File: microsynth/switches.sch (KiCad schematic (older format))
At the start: 35 parts, among them SW12 SOURCE, SW13 THUMBWEEL, SW14 SW_SPDT, SW15 SW_SPDT, SW16 SW_SPDT, SW17 SW_SPDT, SW2 RANGE, SW21 SW_Rotary2x6, SW3 SW_DPTT_SELECTOR, SW4 SW_DPTT_SELECTOR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

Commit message: Tidy up, name switches, proper footprints for all trimmers
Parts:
- RV4, RV7: footprint Potentiometers:Potentiometer_WirePads_Small -> Potentiometers:Potentiometer_Trimmer_Bourns_PV36W
- SW12, SW13, SW3, SW4, SW6: footprint Buttons_Switches_ThroughHole:L203011MS02Q -> Buttons_Switches_ThroughHole:G-1128S-1110
- SW14, SW15, SW16, SW17, SW5: footprint 4ms:SPDT_KIT -> Buttons_Switches_ThroughHole:GF-624-6014
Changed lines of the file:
@@
 F 0 "SW6" H 6294 3079 50  0000 L CNN
 F 1 "SW_DPTT_SELECTOR" H 6294 2988 50  0000 L CNN
-F 2 "Buttons_Switches_ThroughHole:L203011MS02Q" H 6100 2950 50  0001 C CNN
+F 2 "Buttons_Switches_ThroughHole:G-1128S-1110" H 6100 2950 50  0001 C CNN
 F 3 "" H 6100 2950 50  0001 C CNN
 	2    6100 2950
@@
 F 0 "SW3" H 7594 1338 50  0000 L CNN
 F 1 "SW_DPTT_SELECTOR" H 7594 1247 50  0000 L CNN
-F 2 "Buttons_Switches_ThroughHole:L203011MS02Q" H 7400 1350 50  0001 C CNN
+F 2 "Buttons_Switches_ThroughHole:G-1128S-1110" H 7400 1350 50  0001 C CNN
 F 3 "" H 7400 1350 50  0001 C CNN
 	1    7400 1350
@@
 F 0 "SW3" H 7594 1379 50  0000 L CNN
 F 1 "SW_DPTT_SELECTOR" H 7594 1288 50  0000 L CNN
-F 2 "Buttons_Switches_ThroughHole:L203011MS02Q" H 7400 1250 50  0001 C CNN
+F 2 "Buttons_Switches_ThroughHole:G-1128S-1110" H 7400 1250 50  0001 C CNN
 F 3 "" H 7400 1250 50  0001 C CNN
 	2    7400 1250
@@
 F 0 "SW4" H 9344 1338 50  0000 L CNN
 F 1 "SW_DPTT_SELECTOR" H 9344 1247 50  0000 L CNN
-F 2 "Buttons_Switches_ThroughHole:L203011MS02Q" H 9150 1350 50  0001 C CNN
+F 2 "Buttons_Switches_ThroughHole:G-1128S-1110" H 9150 1350 50  0001 C CNN
 F 3 "" H 9150 1350 50  0001 C CNN
 	1    9150 1350
@@
 F 0 "SW4" H 9344 1379 50  0000 L CNN
 F 1 "SW_DPTT_SELECTOR" H 9344 1288 50  0000 L CNN
-F 2 "Buttons_Switches_ThroughHole:L203011MS02Q" H 9150 1250 50  0001 C CNN
+F 2 "Buttons_Switches_ThroughHole:G-1128S-1110" H 9150 1250 50  0001 C CNN
 F 3 "" H 9150 1250 50  0001 C CNN
 	2    9150 1250
@@
 F 0 "SW5" V 10604 1112 50  0000 R CNN
 F 1 "SW_SPDT" V 10695 1112 50  0000 R CNN
-F 2 "4ms:SPDT_KIT" H 10650 1300 50  0001 C CNN
+F 2 "Buttons_Switches_ThroughHole:GF-624-6014" H 10650 1300 50  0001 C CNN
 F 3 "~" H 10650 1300 50  0001 C CNN
 	1    10650 1300
@@
 F 0 "RV4" V 3735 5750 50  0000 C CNN
 F 1 "10k" V 3644 5750 50  0000 C CNN
-F 2 "Potentiometers:Potentiometer_WirePads_Small" H 3850 5750 50  0001 C CNN
+F 2 "Potentiometers:Potentiometer_Trimmer_Bourns_PV36W" H 3850 5750 50  0001 C CNN
 F 3 "~" H 3850 5750 50  0001 C CNN
 	1    3850 5750
@@
 F 0 "RV7" V 4735 6150 50  0000 C CNN
 F 1 "47k" V 4644 6150 50  0000 C CNN
-F 2 "Potentiometers:Potentiometer_WirePads_Small" H 4850 6150 50  0001 C CNN
+F 2 "Potentiometers:Potentiometer_Trimmer_Bourns_PV36W" H 4850 6150 50  0001 C CNN
 F 3 "~" H 4850 6150 50  0001 C CNN
 	1    4850 6150
@@
 F 0 "SW6" H 2894 2738 50  0000 L CNN
 F 1 "SW_DPTT_SELECTOR" H 2894 2647 50  0000 L CNN
-F 2 "Buttons_Switches_ThroughHole:L203011MS02Q" H 2700 2750 50  0001 C CNN
+F 2 "Buttons_Switches_ThroughHole:G-1128S-1110" H 2700 2750 50  0001 C CNN
 F 3 "" H 2700 2750 50  0001 C CNN
 	1    2700 2750
@@
 F 0 "SW17" H 3600 2635 50  0000 C CNN
 F 1 "SW_SPDT" H 3600 2544 50  0000 C CNN
-F 2 "4ms:SPDT_KIT" H 3600 2350 50  0001 C CNN
+F 2 "Buttons_Switches_ThroughHole:GF-624-6014" H 3600 2350 50  0001 C CNN
 F 3 "~" H 3600 2350 50  0001 C CNN
 	1    3600 2350
@@
 F 0 "SW16" H 3600 2135 50  0000 C CNN
 F 1 "SW_SPDT" H 3600 2044 50  0000 C CNN
-F 2 "4ms:SPDT_KIT" H 3600 1850 50  0001 C CNN
+F 2 "Buttons_Switches_ThroughHole:GF-624-6014" H 3600 1850 50  0001 C CNN
 F 3 "~" H 3600 1850 50  0001 C CNN
 	1    3600 1850
@@
 F 0 "SW15" H 3600 1635 50  0000 C CNN
 F 1 "SW_SPDT" H 3600 1544 50  0000 C CNN
-F 2 "4ms:SPDT_KIT" H 3600 1350 50  0001 C CNN
+F 2 "Buttons_Switches_ThroughHole:GF-624-6014" H 3600 1350 50  0001 C CNN
 F 3 "~" H 3600 1350 50  0001 C CNN
 	1    3600 1350
@@
 F 0 "SW14" H 3600 1135 50  0000 C CNN
 F 1 "SW_SPDT" H 3600 1044 50  0000 C CNN
-F 2 "4ms:SPDT_KIT" H 3600 850 50  0001 C CNN
+F 2 "Buttons_Switches_ThroughHole:GF-624-6014" H 3600 850 50  0001 C CNN
 F 3 "~" H 3600 850 50  0001 C CNN
 	1    3600 850
@@
 F 0 "SW12" H 5594 4488 50  0000 L CNN
 F 1 "SOURCE" H 5594 4397 50  0000 L CNN
-F 2 "Buttons_Switches_ThroughHole:L203011MS02Q" H 5400 4500 50  0001 C CNN
+F 2 "Buttons_Switches_ThroughHole:G-1128S-1110" H 5400 4500 50  0001 C CNN
 F 3 "" H 5400 4500 50  0001 C CNN
 	1    5400 4500
@@
 F 0 "SW12" H 5594 4629 50  0000 L CNN
 F 1 "SOURCE" H 5594 4538 50  0000 L CNN
-F 2 "Buttons_Switches_ThroughHole:L203011MS02Q" H 5400 4500 50  0001 C CNN
+F 2 "Buttons_Switches_ThroughHole:G-1128S-1110" H 5400 4500 50  0001 C CNN
 F 3 "" H 5400 4500 50  0001 C CNN
 	2    5400 4500
@@
 F 0 "SW13" H 7394 4438 50  0000 L CNN
 F 1 "THUMBWEEL" H 7394 4347 50  0000 L CNN
-F 2 "Buttons_Switches_ThroughHole:L203011MS02Q" H 7200 4450 50  0001 C CNN
+F 2 "Buttons_Switches_ThroughHole:G-1128S-1110" H 7200 4450 50  0001 C CNN
 F 3 "" H 7200 4450 50  0001 C CNN
 	1    7200 4450
@@
 F 0 "SW13" H 7394 4579 50  0000 L CNN
 F 1 "THUMBWEEL" H 7394 4488 50  0000 L CNN
-F 2 "Buttons_Switches_ThroughHole:L203011MS02Q" H 7200 4450 50  0001 C CNN
+F 2 "Buttons_Switches_ThroughHole:G-1128S-1110" H 7200 4450 50  0001 C CNN
 F 3 "" H 7200 4450 50  0001 C CNN
 	2    7200 4450

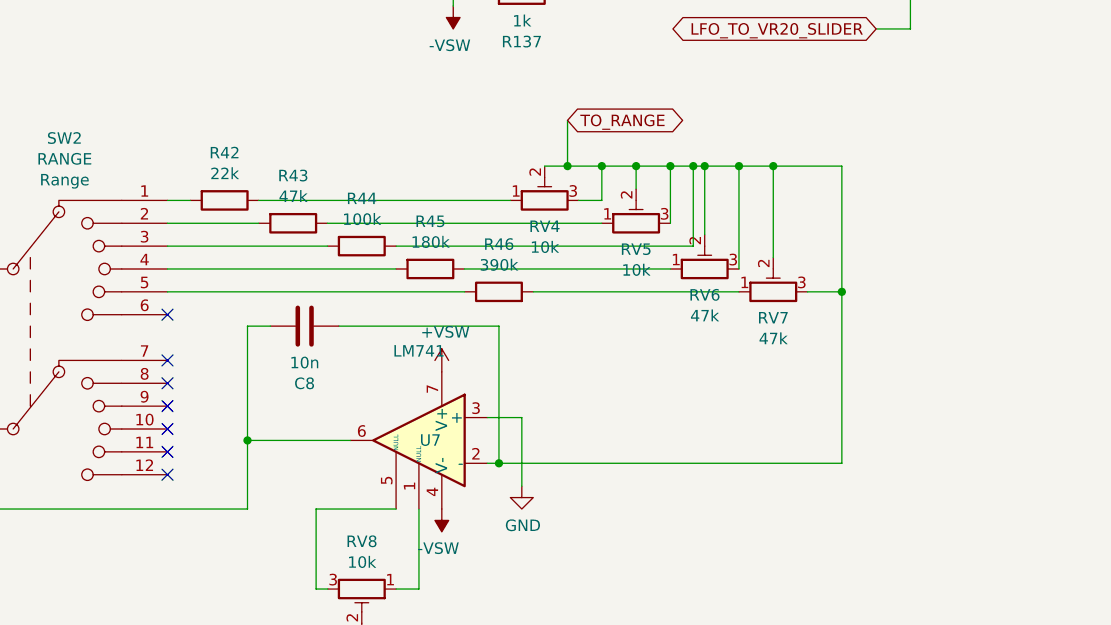
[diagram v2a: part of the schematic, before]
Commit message: Replace switches in schematic, add extra octave to VCO
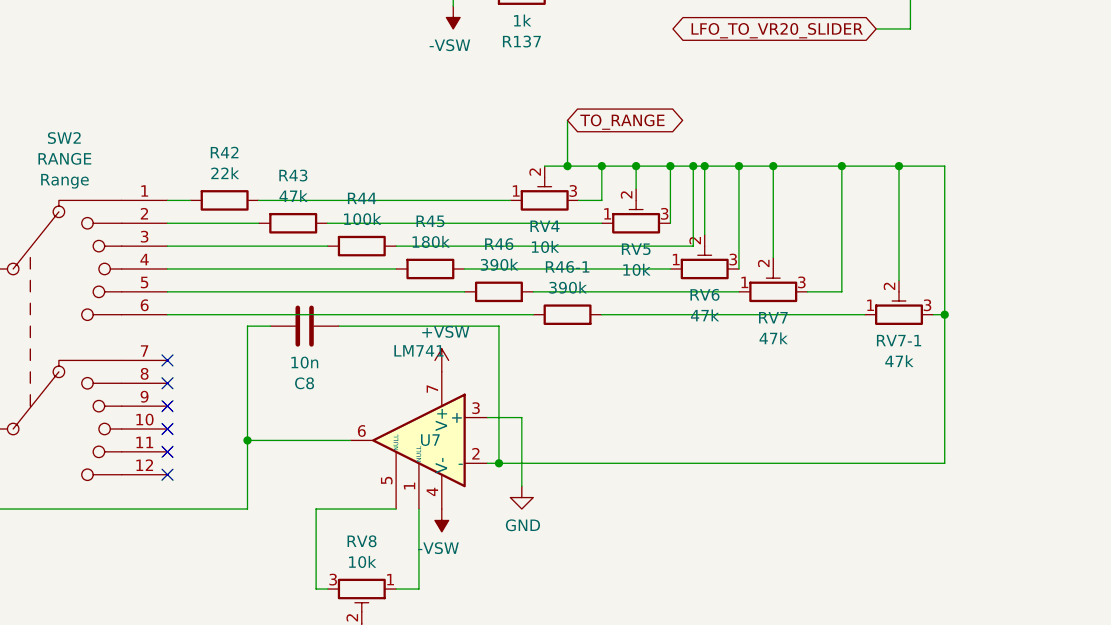
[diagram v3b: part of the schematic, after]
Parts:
- added R46-1: 390k, Resistor_THT:R_Axial_DIN0207_L6.3mm_D2.5mm_P10.16mm_Horizontal, symbol Device:R
- added RV7-1: 47k, Potentiometers:Potentiometer_Trimmer_Bourns_PV36W, symbol Device:R_POT_TRIM
- SW21: footprint MyKi_TH_Panel_Controls:SW_Rotary4+12 -> MyKi_TH_Panel_Controls:LORINCK1049
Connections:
- net TO_RANGE: now also RV7-1.2, RV7-1.3
- net at SW2.6: now also R46-1.1
- new net: R46-1.2, RV7-1.1
- no-connect marks 28 -> 27
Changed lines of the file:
@@
 Wire Wire Line
 	1200 6050 1300 6050
-NoConn ~ 2200 6250
 $Comp
 L Device:R R42
@@
 	2550 7100 2550 6800
 Connection ~ 2550 6800
-Wire Wire Line
-	5150 6150 5150 5600
-Wire Wire Line
-	5150 6900 3650 6900
-Connection ~ 5150 6150
 Connection ~ 3650 6900
 Wire Wire Line
@@
 F 0 "SW21" H 1850 2631 50  0000 C CNN
 F 1 "SW_Rotary2x6" H 1850 2540 50  0000 C CNN
-F 2 "MyKi_TH_Panel_Controls:SW_Rotary4+12" H 1700 2450 50  0001 C CNN
+F 2 "MyKi_TH_Panel_Controls:LORINCK1049" H 1700 2450 50  0001 C CNN
 F 3 "http://cdn-reichelt.de/documents/datenblatt/C200/DS-Serie%23LOR.pdf" H 1700 2450 50  0001 C CNN
 	1    1800 1850
@@
 Connection ~ 5350 4700
 Connection ~ 5350 4300
-Wire Wire Line
-	5150 6150 5150 6900
-Wire Wire Line
-	5150 5600 4850 5600
 Connection ~ 4850 5600
 Wire Wire Line
@@
 Wire Wire Line
 	4750 4600 4750 4800
+$Comp
+L Device:R R46-1
+U 1 1 5EAE5FD2
+P 3950 6250
+F 0 "R46-1" V 4157 6250 50  0000 C CNN
+F 1 "390k" V 4066 6250 50  0000 C CNN
+F 2 "Resistor_THT:R_Axial_DIN0207_L6.3mm_D2.5mm_P10.16mm_Horizontal" V 3880 6250 50  0001 C CNN
+F 3 "~" H 3950 6250 50  0001 C CNN
+	1    3950 6250
+	0    -1   -1   0
+$EndComp
+Wire Wire Line
+	5600 5600 5600 6250
+Wire Wire Line
+	4850 5600 5150 5600
+Wire Wire Line
+	3650 6900 5600 6900
+Wire Wire Line
+	5150 6150 5150 5600
+Connection ~ 5150 5600
+Wire Wire Line
+	5150 5600 5400 5600
+$Comp
+L Device:R_POT_TRIM RV7-1
+U 1 1 5EB1EF45
+P 5400 6250
+F 0 "RV7-1" V 5285 6250 50  0000 C CNN
+F 1 "47k" V 5194 6250 50  0000 C CNN
+F 2 "Potentiometers:Potentiometer_Trimmer_Bourns_PV36W" H 5400 6250 50  0001 C CNN
+F 3 "~" H 5400 6250 50  0001 C CNN
+	1    5400 6250
+	0    -1   -1   0
+$EndComp
+Wire Wire Line
+	5400 6100 5400 5600
+Connection ~ 5400 5600
+Wire Wire Line
+	5400 5600 5600 5600
+Wire Wire Line
+	5550 6250 5600 6250
+Connection ~ 5600 6250
+Wire Wire Line
+	5600 6250 5600 6900
+Wire Wire Line
+	5250 6250 4100 6250
+Wire Wire Line
+	3800 6250 2200 6250
 $EndSCHEMATC

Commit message: Update datasheet for SW2
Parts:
- SW2: Product# (none) -> SR26NS1-2-6-M10-38R6
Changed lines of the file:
@@
 F 1 "RANGE" H 1750 7130 50  0000 C CNN
 F 2 "MyKi_TH_Panel_Controls:SW_Rotary4+12" H 1600 6950 50  0001 C CNN
-F 3 "http://cdn-reichelt.de/documents/datenblatt/C200/DS-Serie%23LOR.pdf" H 1600 6950 50  0001 C CNN
+F 3 "https://www.tme.eu/Document/ecc8d6706892f543e4658b0fb9f5b772/sr261112.pdf" H 1600 6950 50  0001 C CNN
 F 4 "Range" H 1750 7039 50  0000 C CNN "Label"
+F 5 "SR26NS1-2-6-M10-38R6" H 1700 6350 50  0001 C CNN "Product#"
 	1    1700 6350
 	1    0    0    -1

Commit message: Replace SW21 with 3p4t tayda
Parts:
- SW21: footprint MyKi_TH_Panel_Controls:LORINCK1049 -> Button_Switch_THT:SR2612F-0304-18R0B-D8-N; symbol Switch:SW_Rotary2x6 -> Switch:SW_Rotary3x4
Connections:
- net TO_VCA_C27: now also SW21.6; no longer SW21.8
- net TO_VCF_R120: now also SW21.5, SW21.8; no longer SW21.10, SW21.9
- no-connect marks 27 -> 28
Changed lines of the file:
@@
 	2400 2950 2550 2950
 Wire Wire Line
-	2400 2250 2400 2950
-Wire Wire Line
-	2200 2250 2400 2250
+	2400 2050 2400 2950
+Wire Wire Line
+	2200 2050 2400 2050
 $Comp
 L microsynth-rescue:SW_DPTT_SELECTOR-Switch SW6
@@
 	1    0    0    -1
 $EndComp
-NoConn ~ 1300 2450
-NoConn ~ 1300 2350
-NoConn ~ 1300 1750
-NoConn ~ 1300 1650
 NoConn ~ 3800 2450
 NoConn ~ 3800 1950
@@
 $EndComp
 Wire Wire Line
-	1150 1950 1300 1950
-Wire Wire Line
-	1300 2250 1150 2250
-$Comp
-L Switch:SW_Rotary2x6 SW21
-U 1 1 5E476048
-P 1800 1850
-F 0 "SW21" H 1850 2631 50  0000 C CNN
-F 1 "SW_Rotary2x6" H 1850 2540 50  0000 C CNN
-F 2 "MyKi_TH_Panel_Controls:LORINCK1049" H 1700 2450 50  0001 C CNN
-F 3 "http://cdn-reichelt.de/documents/datenblatt/C200/DS-Serie%23LOR.pdf" H 1700 2450 50  0001 C CNN
-	1    1800 1850
-	-1   0    0    -1
-$EndComp
+	1150 1850 1300 1850
+Wire Wire Line
+	1300 2150 1150 2150
 Wire Wire Line
 	2550 1550 2200 1550
@@
 Text GLabel 5800 2550 0    50   BiDi ~ 0
 VCO2_MOD_SWITCH_S6-1
-Text GLabel 1000 2150 0    50   BiDi ~ 0
+Text GLabel 1000 2050 0    50   BiDi ~ 0
 TO_VCF_R120
 Wire Wire Line
-	1150 2250 1150 2150
-Wire Wire Line
-	1150 2150 1150 1950
-Wire Wire Line
-	1150 2150 1300 2150
-Wire Wire Line
-	1000 2150 1150 2150
-Connection ~ 1150 2150
-Text GLabel 1000 2050 0    50   BiDi ~ 0
+	1150 2150 1150 2050
+Wire Wire Line
+	1150 2050 1150 1850
+Wire Wire Line
+	1150 2050 1300 2050
+Wire Wire Line
+	1000 2050 1150 2050
+Connection ~ 1150 2050
+Text GLabel 1000 1950 0    50   BiDi ~ 0
 TO_VCA_C27
 Wire Wire Line
-	1000 2050 1300 2050
-Text GLabel 1300 1250 0    50   BiDi ~ 0
+	1000 1950 1300 1950
+Text GLabel 1300 1350 0    50   BiDi ~ 0
 VCO2_SQR
-Text GLabel 1300 1350 0    50   BiDi ~ 0
+Text GLabel 1300 1450 0    50   BiDi ~ 0
 VCO2_TRI
-Text GLabel 1300 1450 0    50   BiDi ~ 0
+Text GLabel 1300 1550 0    50   BiDi ~ 0
 VCO2_SAW
-Text GLabel 1300 1550 0    50   BiDi ~ 0
+Text GLabel 1300 1650 0    50   BiDi ~ 0
 VCO2_SAW_INV
 Text GLabel 3800 1250 2    50   BiDi ~ 0
@@
 Wire Wire Line
 	3800 6250 2200 6250
+$Comp
+L Switch:SW_Rotary3x4 SW21
+U 1 1 5E476048
+P 1800 2050
+F 0 "SW21" H 1850 2831 50  0000 C CNN
+F 1 "SW_Rotary2x6" H 1850 2740 50  0000 C CNN
+F 2 "Button_Switch_THT:SR2612F-0304-18R0B-D8-N" H 1700 2650 50  0001 C CNN
+F 3 "https://www.taydaelectronics.com/datasheets/A-1891.pdf" H 1700 2650 50  0001 C CNN
+	1    1800 2050
+	-1   0    0    -1
+$EndComp
+NoConn ~ 2200 2550
+NoConn ~ 1300 2350
+NoConn ~ 1300 2450
+NoConn ~ 1300 2550
+NoConn ~ 1300 2650
 $EndSCHEMATC

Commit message: Proper capacitor footprints
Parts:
- C8: footprint Capacitor_THT:C_Disc_D5.0mm_W2.5mm_P5.00mm -> Capacitor_THT:C_Rect_L7.2mm_W2.5mm_P5.00mm_FKS2_FKP2_MKS2_MKP2
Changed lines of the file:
@@
 F 0 "C8" V 3052 6300 50  0000 C CNN
 F 1 "10n" V 2961 6300 50  0000 C CNN
-F 2 "Capacitor_THT:C_Disc_D5.0mm_W2.5mm_P5.00mm" H 2838 6150 50  0001 C CNN
+F 2 "Capacitor_THT:C_Rect_L7.2mm_W2.5mm_P5.00mm_FKS2_FKP2_MKS2_MKP2" H 2838 6150 50  0001 C CNN
 F 3 "~" H 2800 6300 50  0001 C CNN
 	1    2800 6300

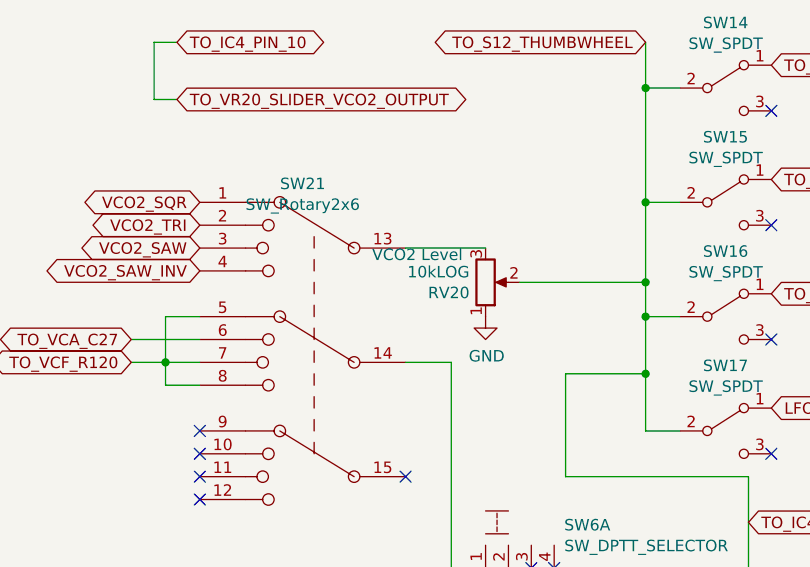
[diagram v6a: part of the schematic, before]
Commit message: Label pots
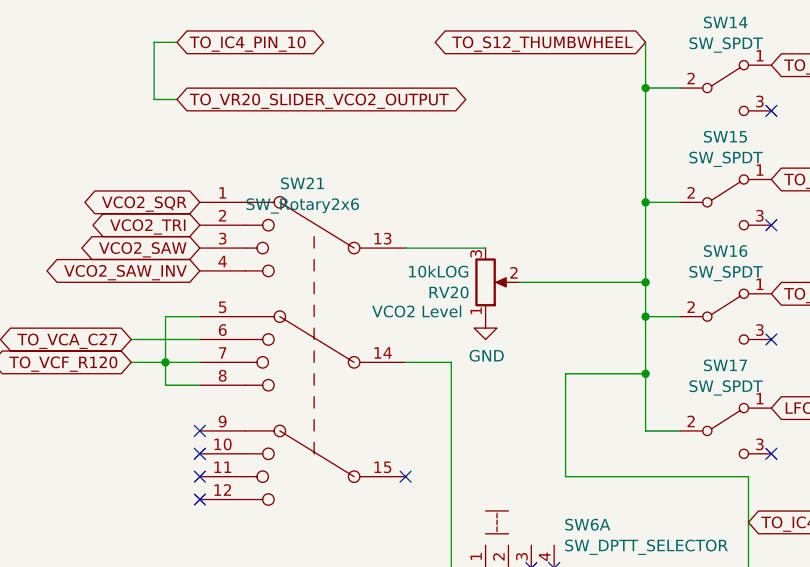
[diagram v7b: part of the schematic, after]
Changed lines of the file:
@@
 F 2 "4ms_Potentiometer:Pot_16mm_NoDet_RV16AF-4A" H 2550 1700 50  0001 C CNN
 F 3 "~" H 2550 1700 50  0001 C CNN
-F 4 "VCO2 Level" H 2450 1550 50  0000 R BNN "Label"
+F 4 "VCO2 Level" H 2450 1800 50  0000 R BNN "Label"
 	1    2550 1700
 	1    0    0    1

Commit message: Replace thumbwheel and cleanup
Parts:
- RV27: footprint 4ms_Potentiometer:Pot_16mm_NoDet_RV16AF-4A -> Potentiometers:Potentiometer_Bourns_PTV09A-2_Vertical
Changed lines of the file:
@@
 F 0 "RV27" H 6330 4796 50  0000 R CNN
 F 1 "4.7kLOG" H 6330 4705 50  0000 R CNN
-F 2 "4ms_Potentiometer:Pot_16mm_NoDet_RV16AF-4A" H 6400 4750 50  0001 C CNN
+F 2 "Potentiometers:Potentiometer_Bourns_PTV09A-2_Vertical" H 6400 4750 50  0001 C CNN
 F 3 "~" H 6400 4750 50  0001 C CNN
 F 4 "Thumbwheel" H 6300 4600 50  0000 R BNN "Label"
